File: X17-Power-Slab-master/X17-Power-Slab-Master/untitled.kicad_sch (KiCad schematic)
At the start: 0 parts

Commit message: Latest Updated Alumni Design Review
Added 48V to 5V DC DC Converter Symbol. Footprint still needed.
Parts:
- added R18: 10000, symbol Device:R_US
- added U5: ~, symbol 48Vto5V_PKU:PKU5311PI
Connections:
- new net: R18.2, U5.3 (Trim)
- new net 48V_GND: U5.2 (In-)
- new net 48V_In: U5.1 (+In)
- new net 5V_GND: R18.1, U5.4 (Out+), U5.5 (Out-)
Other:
- note added: "48V to 5V DCDC Converter"

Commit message: Clarifications
Added clarifications for trim and resistor meant for adjusting output voltage.
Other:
- note added: "Meant for adjusting output voltage, will adjust value later."
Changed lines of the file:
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@@
+		)
+	)
+	(text "Meant for adjusting output voltage, \nwill adjust value later."
+		(exclude_from_sim no)
+		(at 123.952 106.426 0)
+		(effects
+			(font
+				(size 1.27 1.27)
+			)
 		)
 	)

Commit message: Schematic Updates
#SlayedTheDayAway
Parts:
- added R27: 10k, symbol Device:R_US
- R18: value 10000 -> 10k
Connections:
- net 5V_GND: no longer U5.4 (Out+)
- net at R18.2, U5.3 (Trim): now also R27.2
- net 48V_In renamed 48V
- new net 5V_Out1: R27.1, U5.4 (Out+)
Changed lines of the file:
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@@
 	(paper "A4")
 	(junction
-		(at 133.35 97.79)
+		(at 109.22 87.63)
 		(diameter 0)
 		(color 0 0 0 0)
@@
 	(wire
 		(pts
+			(xy 124.46 97.79) (xy 138.43 97.79)
+		)
+		(stroke
+			(width 0)
+			(type default)
+		)
+	)
+	(wire
+		(pts
 			(xy 109.22 97.79) (xy 116.84 97.79)
 		)
@@
 	(wire
 		(pts
-			(xy 133.35 80.01) (xy 133.35 97.79)
+			(xy 132.08 87.63) (xy 138.43 87.63)
+		)
+		(stroke
+			(width 0)
+			(type default)
+		)
+	)
+	(wire
+		(pts
+			(xy 97.79 87.63) (xy 97.79 104.14)
+		)
+		(stroke
+			(width 0)
+			(type default)
+		)
+	)
+	(wire
+		(pts
+			(xy 109.22 87.63) (xy 109.22 97.79)
+		)
+		(stroke
+			(width 0)
+			(type default)
+		)
+	)
+	(wire
+		(pts
+			(xy 133.35 80.01) (xy 133.35 104.14)
+		)
+		(stroke
+			(width 0)
+			(type default)
+		)
+	)
+	(wire
+		(pts
+			(xy 138.43 87.63) (xy 138.43 97.79)
+		)
+		(stroke
+			(width 0)
+			(type default)
+		)
+	)
+	(wire
+		(pts
+			(xy 97.79 87.63) (xy 109.22 87.63)
+		)
+		(stroke
+			(width 0)
+			(type default)
+		)
+	)
+	(wire
+		(pts
+			(xy 97.79 104.14) (xy 125.73 104.14)
+		)
+		(stroke
+			(width 0)
+			(type default)
+		)
+	)
+	(wire
+		(pts
+			(xy 138.43 87.63) (xy 140.97 87.63)
+		)
+		(stroke
+			(width 0)
+			(type default)
+		)
+	)
+	(wire
+		(pts
+			(xy 132.08 80.01) (xy 133.35 80.01)
 		)
 		(stroke
@@
 		(pts
 			(xy 133.35 80.01) (xy 140.97 80.01)
-		)
-		(stroke
-			(width 0)
-			(type default)
-		)
-	)
-	(wire
-		(pts
-			(xy 132.08 87.63) (xy 138.43 87.63)
-		)
-		(stroke
-			(width 0)
-			(type default)
-		)
-	)
-	(wire
-		(pts
-			(xy 124.46 97.79) (xy 133.35 97.79)
-		)
-		(stroke
-			(width 0)
-			(type default)
-		)
-	)
-	(wire
-		(pts
-			(xy 109.22 87.63) (xy 109.22 97.79)
-		)
-		(stroke
-			(width 0)
-			(type default)
-		)
-	)
-	(wire
-		(pts
-			(xy 138.43 87.63) (xy 138.43 97.79)
-		)
-		(stroke
-			(width 0)
-			(type default)
-		)
-	)
-	(wire
-		(pts
-			(xy 138.43 87.63) (xy 140.97 87.63)
-		)
-		(stroke
-			(width 0)
-			(type default)
-		)
-	)
-	(wire
-		(pts
-			(xy 133.35 97.79) (xy 138.43 97.79)
-		)
-		(stroke
-			(width 0)
-			(type default)
-		)
-	)
-	(wire
-		(pts
-			(xy 132.08 80.01) (xy 133.35 80.01)
 		)
 		(stroke
@@
 	(text "Meant for adjusting output voltage, \nwill adjust value later."
 		(exclude_from_sim no)
-		(at 123.952 106.426 0)
+		(at 122.682 109.728 0)
 		(effects
 			(font
@@
 		)
 	)
-	(global_label "48V_In"
+	(global_label "48V"
 		(shape input)
 		(at 109.22 80.01 180)
@@
 		)
 		(property "Intersheetrefs" "${INTERSHEET_REFS}"
-			(at 100.0058 80.01 0)
+			(at 102.7272 80.01 0)
 			(effects
 				(font
@@
 				(justify right)
 				(hide yes)
+			)
+		)
+	)
+	(symbol
+		(lib_id "Device:R_US")
+		(at 129.54 104.14 270)
+		(unit 1)
+		(exclude_from_sim no)
+		(in_bom yes)
+		(on_board yes)
+		(dnp no)
+		(fields_autoplaced yes)
+		(property "Reference" "R27"
+			(at 129.54 97.79 90)
+			(effects
+				(font
+					(size 1.27 1.27)
+				)
+			)
+		)
+		(property "Value" "10k"
+			(at 129.54 100.33 90)
+			(effects
+				(font
+					(size 1.27 1.27)
+				)
+			)
+		)
+		(property "Footprint" ""
+			(at 129.286 105.156 90)
+			(effects
+				(font
+					(size 1.27 1.27)
+				)
+				(hide yes)
+			)
+		)
+		(property "Datasheet" "~"
+			(at 129.54 104.14 0)
+			(effects
+				(font
+					(size 1.27 1.27)
+				)
+				(hide yes)
+			)
+		)
+		(property "Description" "Resistor, US symbol"
+			(at 129.54 104.14 0)
+			(effects
+				(font
+					(size 1.27 1.27)
+				)
+				(hide yes)
+			)
+		)
+		(pin "1"
+		)
+		(pin "2"
+		)
+		(instances
+			(project "X17-Power-Slab-Master"
+				(path "/57e59c68-7be1-495e-b535-e78e0f561e15/bdfdae5a-9acb-4759-8fe8-e68c48f1ce0d"
+					(reference "R27")
+					(unit 1)
+				)
 			)
 		)
@@
 			)
 		)
-		(property "Value" "10000"
+		(property "Value" "10k"
 			(at 120.65 93.98 90)
 			(effects

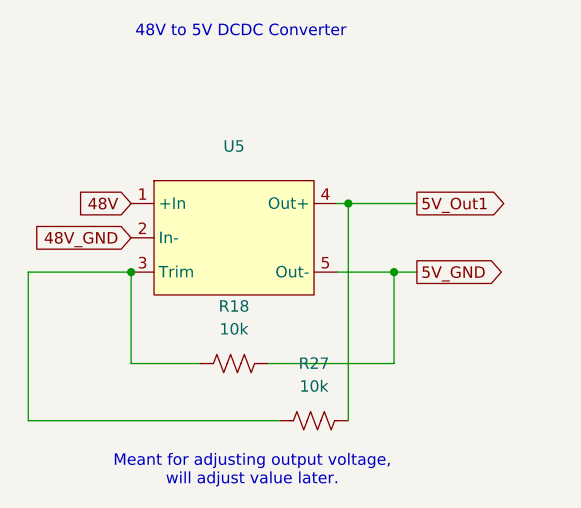
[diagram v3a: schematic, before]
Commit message: Schematic Full Update
Probs can start pacing after this.
Diode on RVP changed,
Button changed
Reverse voltage updated
Symbols updated to remove DRCs
GNDs changed
Connector updated
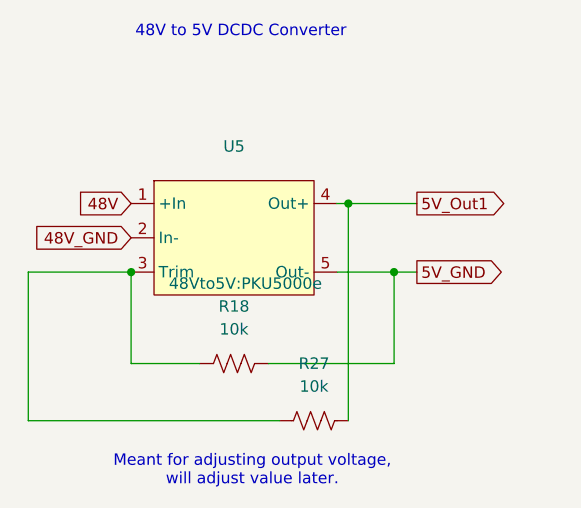
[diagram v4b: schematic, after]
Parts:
- R18, R27: footprint (none) -> Resistor_SMD:R_0603_1608Metric_Pad0.98x0.95mm_HandSolder
- U5: footprint (none) -> 48Vto5V:PKU5000e
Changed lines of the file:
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@@
 			)
 		)
-		(property "Footprint" ""
+		(property "Footprint" "Resistor_SMD:R_0603_1608Metric_Pad0.98x0.95mm_HandSolder"
 			(at 129.286 105.156 90)
 			(effects
@@
 			)
 		)
-		(property "Footprint" ""
+		(property "Footprint" "Resistor_SMD:R_0603_1608Metric_Pad0.98x0.95mm_HandSolder"
 			(at 120.396 98.806 90)
 			(effects
@@
 			)
 		)
-		(property "Footprint" ""
+		(property "Footprint" "48Vto5V:PKU5000e"
 			(at 121.92 88.9 0)
 			(effects
@@
 					(size 1.27 1.27)
 				)
-				(hide yes)
 			)
 		)

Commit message: Final First(?) Draft
NRST is stuck to general ground for whatever reason.

Test points wont connect for the life of me, will look @ in morning, will have sample plan.

Idea is there, really want to plan it out better 2nd time around. Alumni will give good tips!
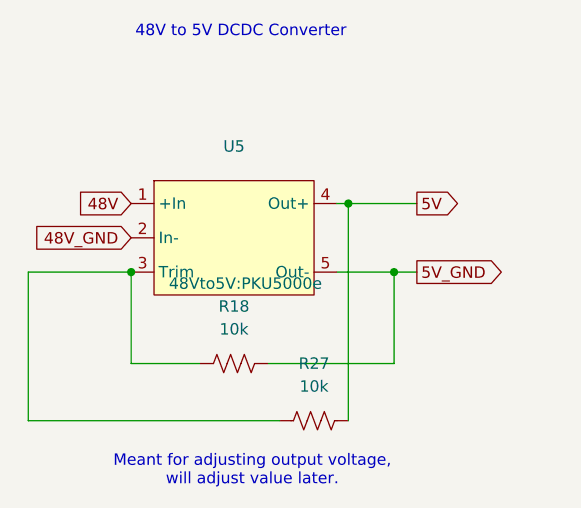
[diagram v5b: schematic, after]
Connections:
- net 5V_Out1 renamed 5V
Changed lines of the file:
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@@
 		)
 	)
-	(global_label "5V_Out1"
+	(global_label "5V"
 		(shape output)
 		(at 140.97 80.01 0)
@@
 		)
 		(property "Intersheetrefs" "${INTERSHEET_REFS}"
-			(at 151.6356 80.01 0)
+			(at 146.2533 80.01 0)
 			(effects
 				(font

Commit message: Power traces update
I think I'm getting the idea of power traces needed?
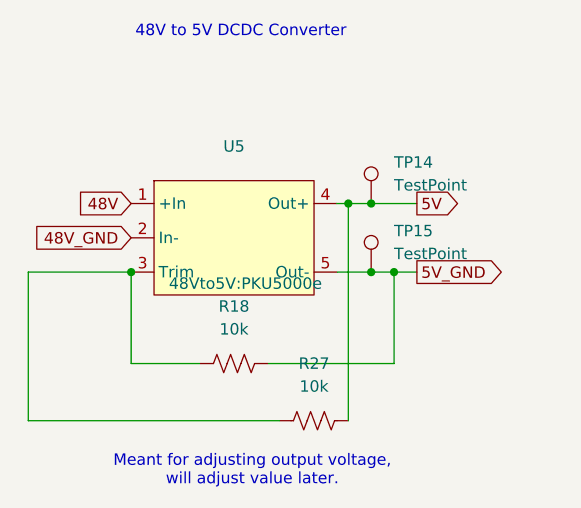
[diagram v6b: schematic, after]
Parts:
- added TP14, TP15: TestPoint, TestPoint:TestPoint_Pad_D4.0mm, symbol Connector:TestPoint
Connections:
- net 5V: now also TP14.1
- net 5V_GND: now also TP15.1
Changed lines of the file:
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@@
 	(paper "A4")
+	(junction
+		(at 135.89 87.63)
+		(diameter 0)
+		(color 0 0 0 0)
+	)
 	(junction
 		(at 109.22 87.63)
@@
 	)
 	(junction
+		(at 135.89 80.01)
+		(diameter 0)
+		(color 0 0 0 0)
+	)
+	(junction
 		(at 138.43 87.63)
 		(diameter 0)
@@
 	(wire
 		(pts
-			(xy 132.08 87.63) (xy 138.43 87.63)
+			(xy 132.08 87.63) (xy 135.89 87.63)
+		)
+		(stroke
+			(width 0)
+			(type default)
+		)
+	)
+	(wire
+		(pts
+			(xy 135.89 87.63) (xy 138.43 87.63)
 		)
 		(stroke
@@
 	(wire
 		(pts
-			(xy 133.35 80.01) (xy 140.97 80.01)
+			(xy 135.89 80.01) (xy 140.97 80.01)
+		)
+		(stroke
+			(width 0)
+			(type default)
+		)
+	)
+	(wire
+		(pts
+			(xy 133.35 80.01) (xy 135.89 80.01)
 		)
 		(stroke
@@
 				(justify right)
 				(hide yes)
+			)
+		)
+	)
+	(symbol
+		(lib_id "Connector:TestPoint")
+		(at 135.89 87.63 0)
+		(unit 1)
+		(exclude_from_sim no)
+		(in_bom yes)
+		(on_board yes)
+		(dnp no)
+		(fields_autoplaced yes)
+		(property "Reference" "TP15"
+			(at 138.43 83.0579 0)
+			(effects
+				(font
+					(size 1.27 1.27)
+				)
+				(justify left)
+			)
+		)
+		(property "Value" "TestPoint"
+			(at 138.43 85.5979 0)
+			(effects
+				(font
+					(size 1.27 1.27)
+				)
+				(justify left)
+			)
+		)
+		(property "Footprint" "TestPoint:TestPoint_Pad_D4.0mm"
+			(at 140.97 87.63 0)
+			(effects
+				(font
+					(size 1.27 1.27)
+				)
+				(hide yes)
+			)
+		)
+		(property "Datasheet" "~"
+			(at 140.97 87.63 0)
+			(effects
+				(font
+					(size 1.27 1.27)
+				)
+				(hide yes)
+			)
+		)
+		(property "Description" "test point"
+			(at 135.89 87.63 0)
+			(effects
+				(font
+					(size 1.27 1.27)
+				)
+				(hide yes)
+			)
+		)
+		(pin "1"
+		)
+		(instances
+			(project "X17-Power-Slab-Master"
+				(path "/57e59c68-7be1-495e-b535-e78e0f561e15/bdfdae5a-9acb-4759-8fe8-e68c48f1ce0d"
+					(reference "TP15")
+					(unit 1)
+				)
 			)
 		)
@@
 					(unit 1)
 				)
+			)
+		)
+	)
+	(symbol
+		(lib_id "Connector:TestPoint")
+		(at 135.89 80.01 0)
+		(unit 1)
+		(exclude_from_sim no)
+		(in_bom yes)
+		(on_board yes)
+		(dnp no)
+		(fields_autoplaced yes)
+		(property "Reference" "TP14"
+			(at 138.43 75.4379 0)
+			(effects
+				(font
+					(size 1.27 1.27)
+				)
+				(justify left)
+			)
+		)
+		(property "Value" "TestPoint"
+			(at 138.43 77.9779 0)
+			(effects
+				(font
+					(size 1.27 1.27)
+				)
+				(justify left)
+			)
+		)
+		(property "Footprint" "TestPoint:TestPoint_Pad_D4.0mm"
+			(at 140.97 80.01 0)
+			(effects
+				(font
+					(size 1.27 1.27)
+				)
+				(hide yes)
+			)
+		)
+		(property "Datasheet" "~"
+			(at 140.97 80.01 0)
+			(effects
+				(font
+					(size 1.27 1.27)
+				)
+				(hide yes)
+			)
+		)
+		(property "Description" "test point"
+			(at 135.89 80.01 0)
+			(effects
+				(font
+					(size 1.27 1.27)
+				)
+				(hide yes)
+			)
+		)
+		(pin "1"
+		)
+		(instances
+			(project "X17-Power-Slab-Master"
+				(path "/57e59c68-7be1-495e-b535-e78e0f561e15/bdfdae5a-9acb-4759-8fe8-e68c48f1ce0d"
+					(reference "TP14")
+					(unit 1)
+				)

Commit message: Power slab delivery changes
Not done yet
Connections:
- net 5V_GND renamed 12V_5V_GND
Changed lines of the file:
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@@
 		)
 	)
-	(global_label "5V_GND"
+	(global_label "12V_5V_GND"
 		(shape output)
 		(at 140.97 87.63 0)
@@
 		)
 		(property "Intersheetrefs" "${INTERSHEET_REFS}"
-			(at 151.0914 87.63 0)
+			(at 155.5666 87.63 0)
 			(effects
 				(font

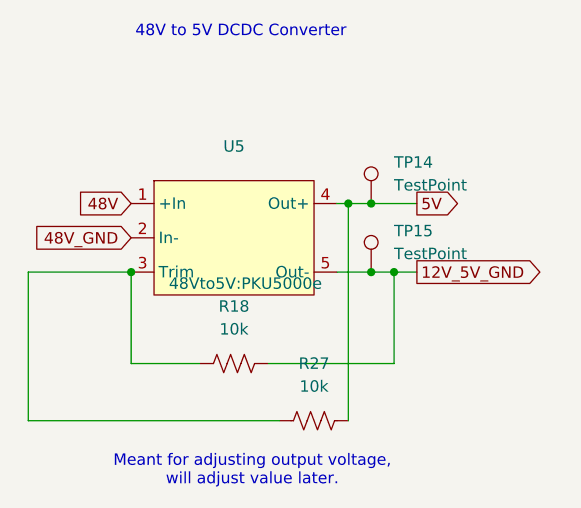
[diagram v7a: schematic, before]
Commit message: Connector pins renamed and attempt @ fixing airwires for 5V Brick
Still don't understand why the airwire from 5V to 12V_5V_GND test point exists, I also now have airwires across all my P08_1 pins despite the same set up existing for 12V.
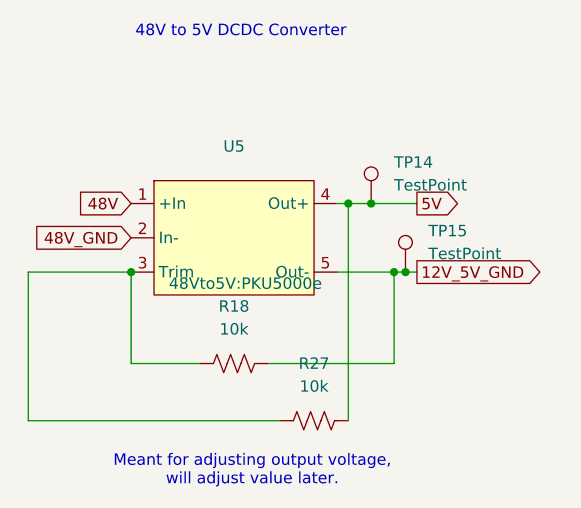
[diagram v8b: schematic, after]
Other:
- moved on the sheet: TP15
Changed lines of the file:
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@@
 	(paper "A4")
 	(junction
-		(at 135.89 87.63)
+		(at 139.7 87.63)
 		(diameter 0)
 		(color 0 0 0 0)
@@
 	(wire
 		(pts
-			(xy 132.08 87.63) (xy 135.89 87.63)
-		)
-		(stroke
-			(width 0)
-			(type default)
-		)
-	)
-	(wire
-		(pts
-			(xy 135.89 87.63) (xy 138.43 87.63)
+			(xy 139.7 87.63) (xy 140.97 87.63)
+		)
+		(stroke
+			(width 0)
+			(type default)
+		)
+	)
+	(wire
+		(pts
+			(xy 132.08 87.63) (xy 138.43 87.63)
 		)
 		(stroke
@@
 	(wire
 		(pts
-			(xy 138.43 87.63) (xy 140.97 87.63)
+			(xy 138.43 87.63) (xy 139.7 87.63)
 		)
 		(stroke
@@
 	(symbol
 		(lib_id "Connector:TestPoint")
-		(at 135.89 87.63 0)
+		(at 139.7 87.63 0)
 		(unit 1)
 		(exclude_from_sim no)
@@
 		(fields_autoplaced yes)
 		(property "Reference" "TP15"
-			(at 138.43 83.0579 0)
+			(at 142.24 83.0579 0)
 			(effects
 				(font
@@
 		)
 		(property "Value" "TestPoint"
-			(at 138.43 85.5979 0)
+			(at 142.24 85.5979 0)
 			(effects
 				(font
@@
 		)
 		(property "Footprint" "TestPoint:TestPoint_Pad_D4.0mm"
-			(at 140.97 87.63 0)
+			(at 144.78 87.63 0)
 			(effects
 				(font
@@
 		)
 		(property "Datasheet" "~"
-			(at 140.97 87.63 0)
+			(at 144.78 87.63 0)
 			(effects
 				(font
@@
 		)
 		(property "Description" "test point"
-			(at 135.89 87.63 0)
-			(effects
-				(font
+			(at 139.7 87.63 0)
+			(effects
+				(font
